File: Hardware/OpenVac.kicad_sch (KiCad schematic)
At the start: 5 parts, among them J1 Conn_01x02, J2 Conn_01x02, U1 ESP32-S3-MINI-1, U2 ESP32-S3-DevKitC

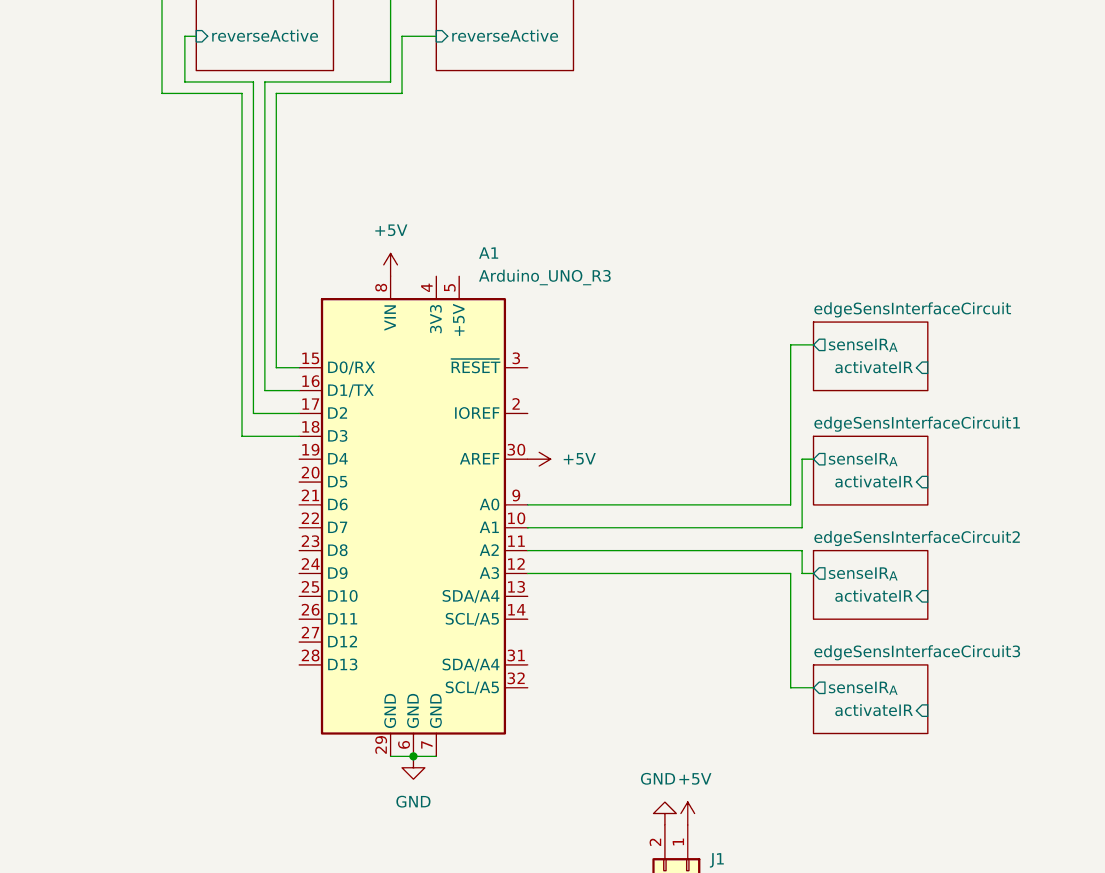
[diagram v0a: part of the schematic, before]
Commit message: fix: mosfet orientation
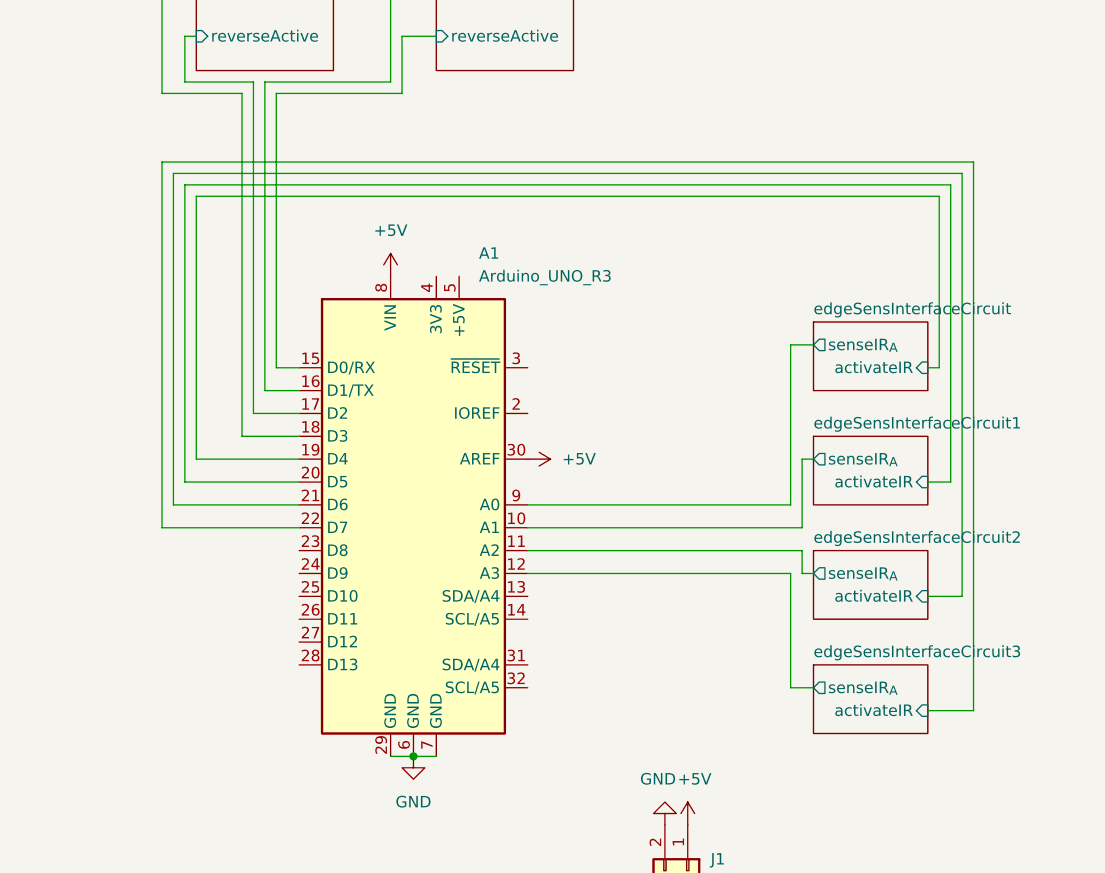
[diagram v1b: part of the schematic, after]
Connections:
- net edgeSensInterfaceCircuit/activateIR: now also A1.19 (D4)
- net edgeSensInterfaceCircuit1/activateIR: now also A1.20 (D5)
- net edgeSensInterfaceCircuit2/activateIR: now also A1.21 (D6)
- net edgeSensInterfaceCircuit3/activateIR: now also A1.22 (D7)
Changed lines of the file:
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@@
+	(wire
+		(pts
+			(xy 203.2 57.15) (xy 115.57 57.15)
+		)
+		(stroke
+			(width 0)
+			(type default)
+		)
+	)
+	(wire
+		(pts
+			(xy 199.39 104.14) (xy 203.2 104.14)
+		)
+		(stroke
+			(width 0)
+			(type default)
+		)
+	)
 	(wire
 		(pts
@@
 	(wire
 		(pts
+			(xy 118.11 88.9) (xy 129.54 88.9)
+		)
+		(stroke
+			(width 0)
+			(type default)
+		)
+	)
+	(wire
+		(pts
 			(xy 185.42 101.6) (xy 186.69 101.6)
 		)
@@
 	(wire
 		(pts
+			(xy 204.47 116.84) (xy 204.47 55.88)
+		)
+		(stroke
+			(width 0)
+			(type default)
+		)
+	)
+	(wire
+		(pts
+			(xy 114.3 55.88) (xy 114.3 96.52)
+		)
+		(stroke
+			(width 0)
+			(type default)
+		)
+	)
+	(wire
+		(pts
+			(xy 201.93 91.44) (xy 201.93 58.42)
+		)
+		(stroke
+			(width 0)
+			(type default)
+		)
+	)
+	(wire
+		(pts
+			(xy 199.39 116.84) (xy 204.47 116.84)
+		)
+		(stroke
+			(width 0)
+			(type default)
+		)
+	)
+	(wire
+		(pts
+			(xy 115.57 57.15) (xy 115.57 93.98)
+		)
+		(stroke
+			(width 0)
+			(type default)
+		)
+	)
+	(wire
+		(pts
 			(xy 116.84 41.91) (xy 116.84 46.99)
 		)
@@
 	(wire
 		(pts
+			(xy 114.3 96.52) (xy 129.54 96.52)
+		)
+		(stroke
+			(width 0)
+			(type default)
+		)
+	)
+	(wire
+		(pts
 			(xy 185.42 96.52) (xy 185.42 88.9)
 		)
@@
 	(wire
 		(pts
+			(xy 204.47 55.88) (xy 114.3 55.88)
+		)
+		(stroke
+			(width 0)
+			(type default)
+		)
+	)
+	(wire
+		(pts
+			(xy 116.84 91.44) (xy 129.54 91.44)
+		)
+		(stroke
+			(width 0)
+			(type default)
+		)
+	)
+	(wire
+		(pts
 			(xy 154.94 99.06) (xy 185.42 99.06)
 		)
@@
 	(wire
 		(pts
+			(xy 203.2 104.14) (xy 203.2 57.15)
+		)
+		(stroke
+			(width 0)
+			(type default)
+		)
+	)
+	(wire
+		(pts
 			(xy 144.78 36.83) (xy 139.7 36.83)
 		)
@@
 	(wire
 		(pts
+			(xy 199.39 91.44) (xy 201.93 91.44)
+		)
+		(stroke
+			(width 0)
+			(type default)
+		)
+	)
+	(wire
+		(pts
+			(xy 115.57 93.98) (xy 129.54 93.98)
+		)
+		(stroke
+			(width 0)
+			(type default)
+		)
+	)
+	(wire
+		(pts
+			(xy 200.66 78.74) (xy 200.66 59.69)
+		)
+		(stroke
+			(width 0)
+			(type default)
+		)
+	)
+	(wire
+		(pts
 			(xy 125.73 46.99) (xy 125.73 81.28)
 		)
@@
 	(wire
 		(pts
+			(xy 200.66 59.69) (xy 118.11 59.69)
+		)
+		(stroke
+			(width 0)
+			(type default)
+		)
+	)
+	(wire
+		(pts
+			(xy 199.39 78.74) (xy 200.66 78.74)
+		)
+		(stroke
+			(width 0)
+			(type default)
+		)
+	)
+	(wire
+		(pts
 			(xy 184.15 76.2) (xy 186.69 76.2)
 		)
@@
 	(wire
 		(pts
+			(xy 118.11 59.69) (xy 118.11 88.9)
+		)
+		(stroke
+			(width 0)
+			(type default)
+		)
+	)
+	(wire
+		(pts
 			(xy 139.7 46.99) (xy 125.73 46.99)
 		)
@@
 	(wire
 		(pts
+			(xy 201.93 58.42) (xy 116.84 58.42)
+		)
+		(stroke
+			(width 0)
+			(type default)
+		)
+	)
+	(wire
+		(pts
 			(xy 140.97 41.91) (xy 140.97 48.26)
 		)
 		(stroke
+			(width 0)
+			(type default)
+		)
+	)
+	(wire
+		(pts
+			(xy 116.84 58.42) (xy 116.84 91.44)
+		)
+		(stroke

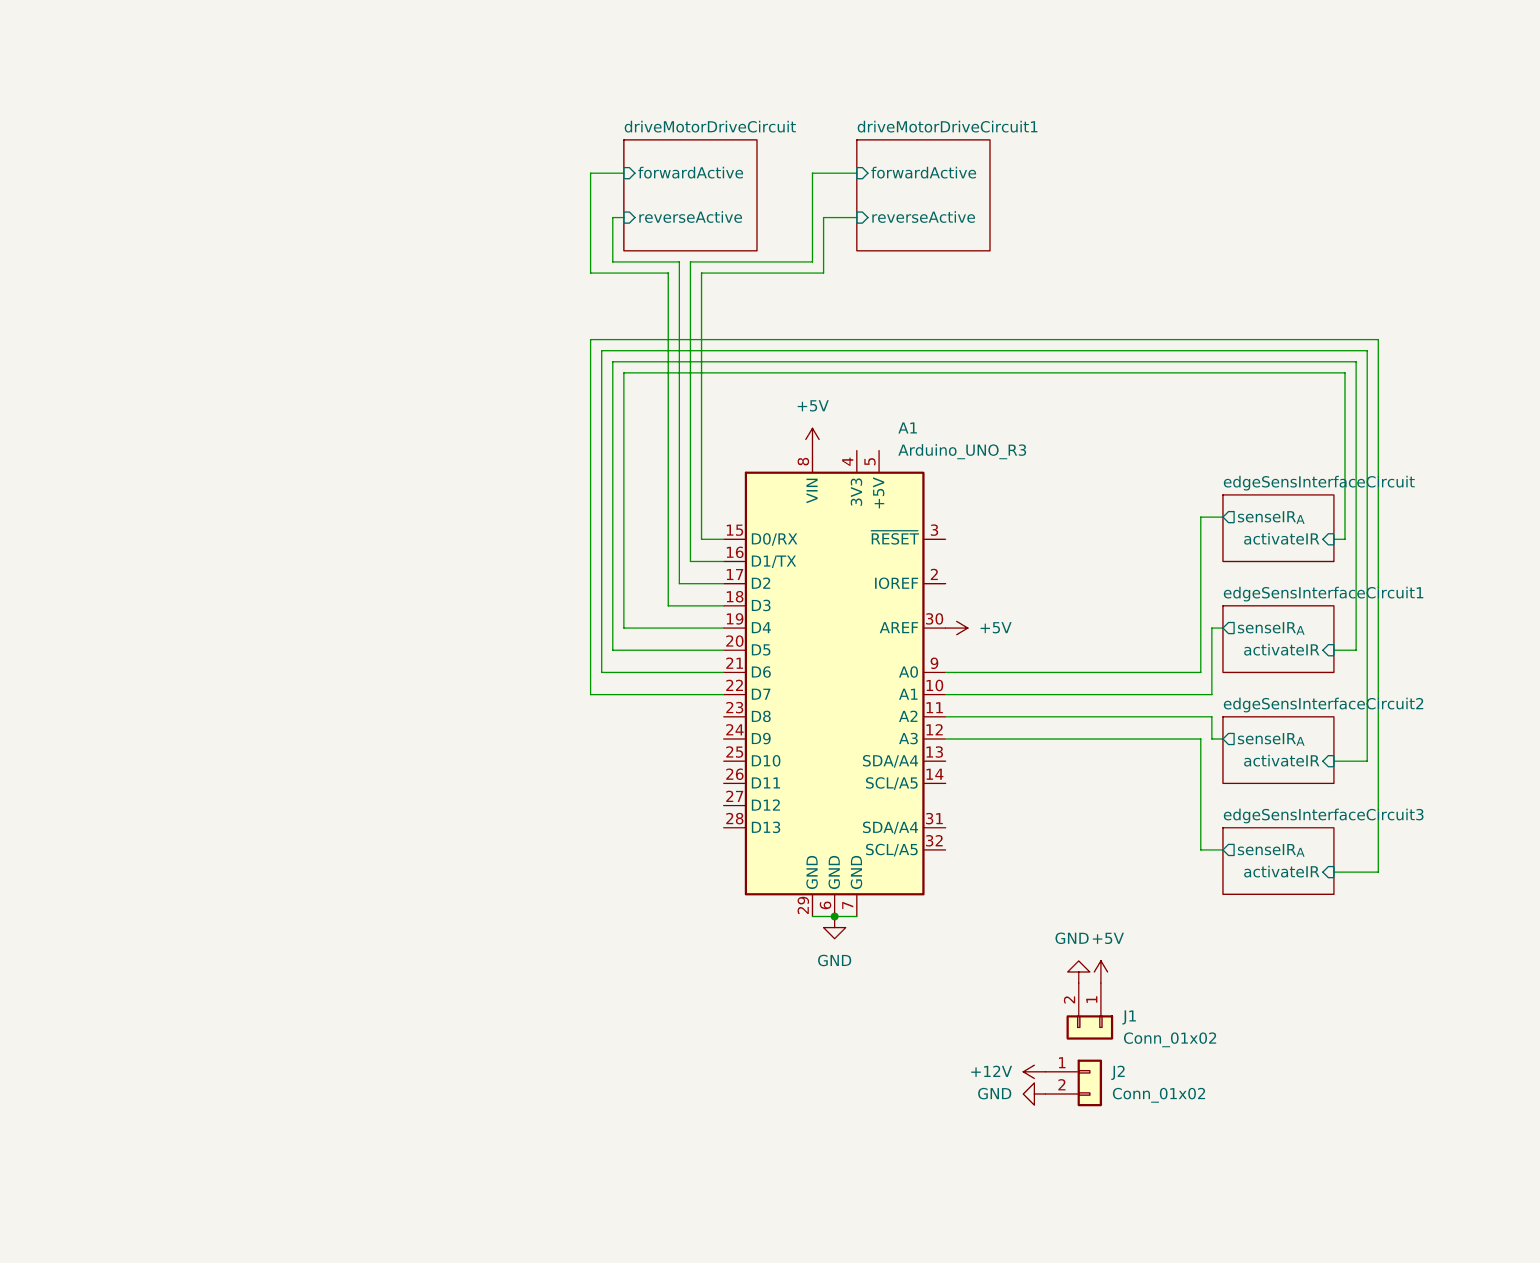
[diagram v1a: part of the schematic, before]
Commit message: feat: all motors and main turbine wired in
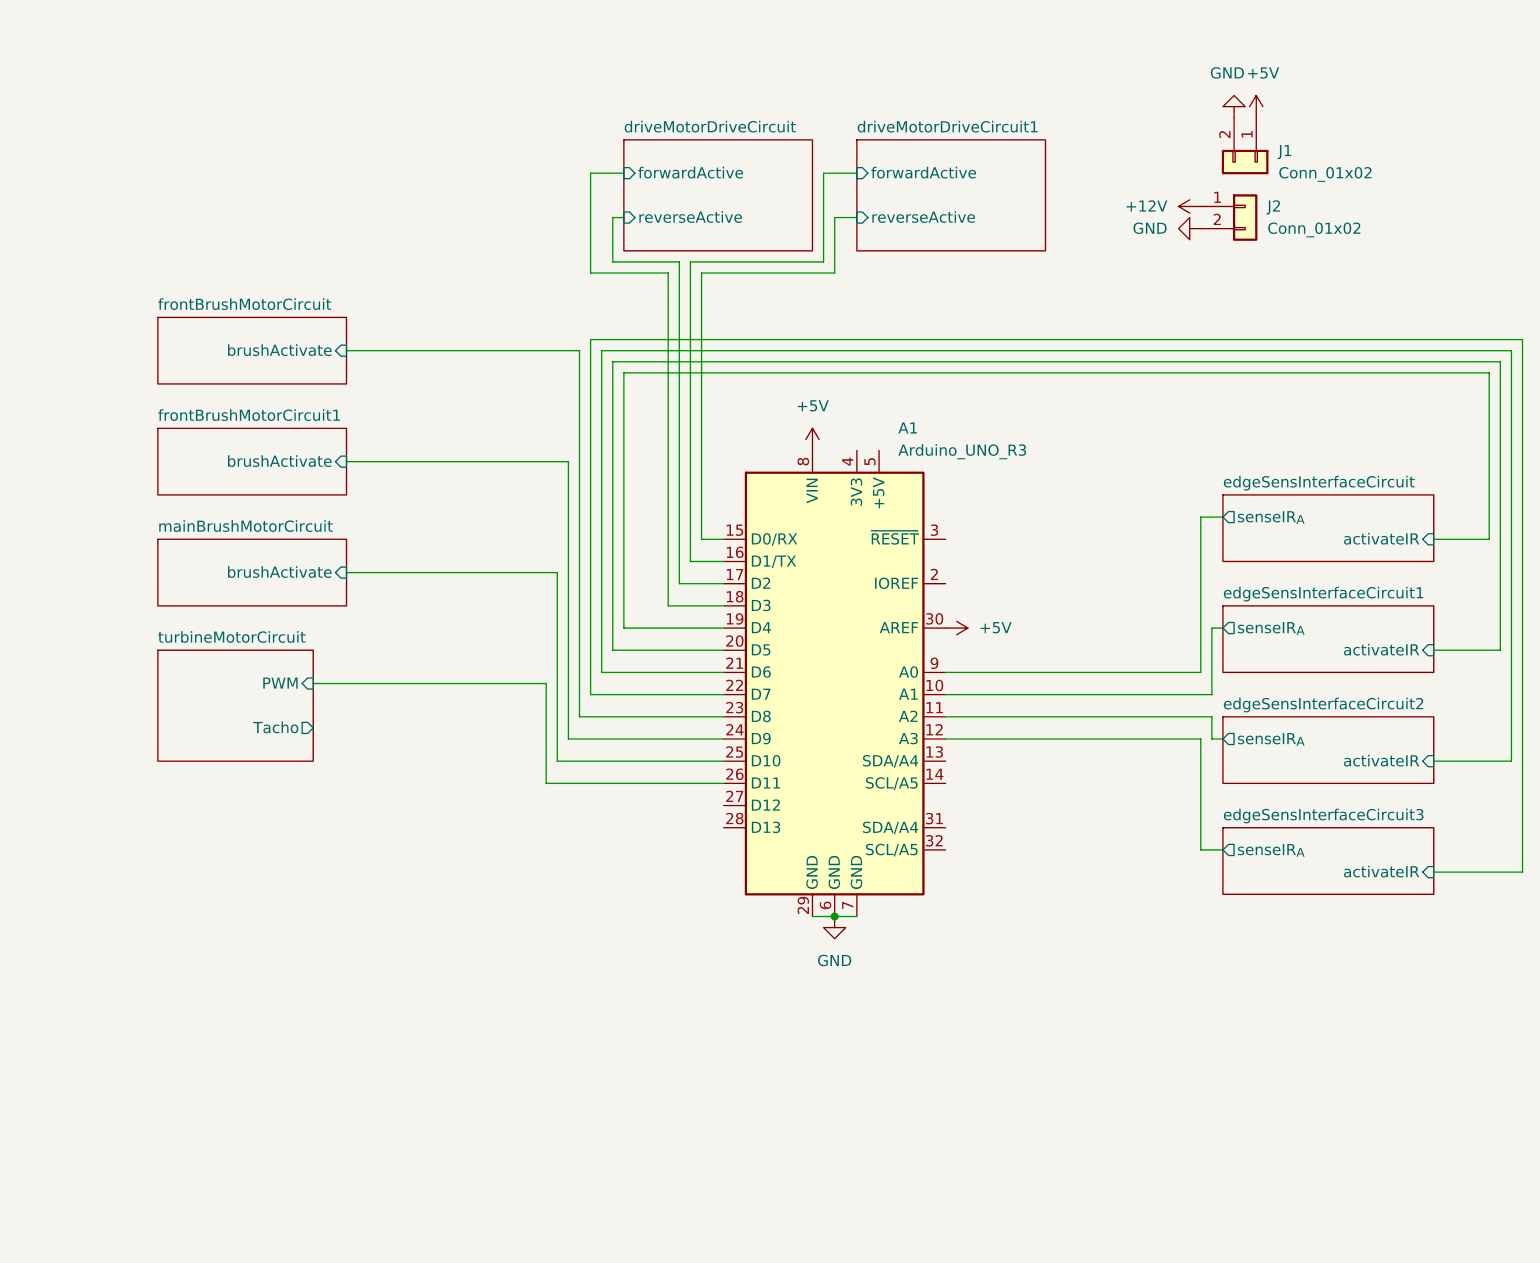
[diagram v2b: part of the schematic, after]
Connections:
- net frontBrushMotorCircuit/brushActivate: now reaches A1.23 (D8)
- net frontBrushMotorCircuit1/brushActivate: now reaches A1.24 (D9)
- net mainBrushMotorCircuit/brushActivate: now reaches A1.25 (D10)
- net turbineMotorCircuit/PWM: now reaches A1.26 (D11)
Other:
- added sheet frontBrushMotorCircuit (front-brush-motor-circuit.kicad_sch)
- added sheet frontBrushMotorCircuit1 (front-brush-motor-circuit.kicad_sch)
- added sheet mainBrushMotorCircuit (front-brush-motor-circuit.kicad_sch)
- added sheet turbineMotorCircuit (turbine-motor-circuit.kicad_sch)
- moved on the sheet: J1, J2

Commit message: Session 13 hardware modifications
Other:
- added sheet bumperArrayInterfaceCircuit (bumper-array-interface-circuit.kicad_sch)
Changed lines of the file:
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@@
+	)
+	(sheet
+		(at 64.77 110.49)
+		(size 38.1 15.24)
+		(fields_autoplaced yes)
+		(stroke
+			(width 0.1524)
+			(type solid)
+		)
+		(fill
+			(color 0 0 0 0.0000)
+		)
+		(property "Sheetname" "bumperArrayInterfaceCircuit"
+			(at 64.77 109.7784 0)
+			(effects
+				(font
+					(size 1.27 1.27)
+				)
+				(justify left bottom)
+			)
+		)
+		(property "Sheetfile" "bumper-array-interface-circuit.kicad_sch"
+			(at 64.77 126.3146 0)
+			(effects
+				(font
+					(size 1.27 1.27)
+				)
+				(justify left top)
+				(hide yes)
+			)
+		)
+		(instances
+			(project "OpenVac"
+				(path "/cfb1a53c-1978-4730-a380-294525b876d3"
+					(page "16")
+				)
+			)
+		)
 	)
 	(sheet
